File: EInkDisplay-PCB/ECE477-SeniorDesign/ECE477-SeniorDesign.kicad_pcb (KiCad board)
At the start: 4 copper layers, 89.2 x 77.8 mm, 95 parts, among them J1 Conn_01x05_Pin, J10 JST Conn, J12 JST Conn, J2 Conn_01x05_Pin, J3 Conn_01x05_Pin, J4 Conn_01x05_Pin, J6 Battery Connector, J7 USB_A, J8 JST Conn, J9 JST Conn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

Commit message: push
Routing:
- net /USB-UART/USB_D+: track 12.9 -> 24.9 mm, vias 1 -> 2
- net /USB-UART/USB_D-: track 11.4 -> 22.6 mm, vias 1 -> 2
- net VBUS: track 24.8 -> 35.3 mm, vias 0 -> 2
- net GND: track 99.3 -> 100.6 mm, vias 46 -> 47

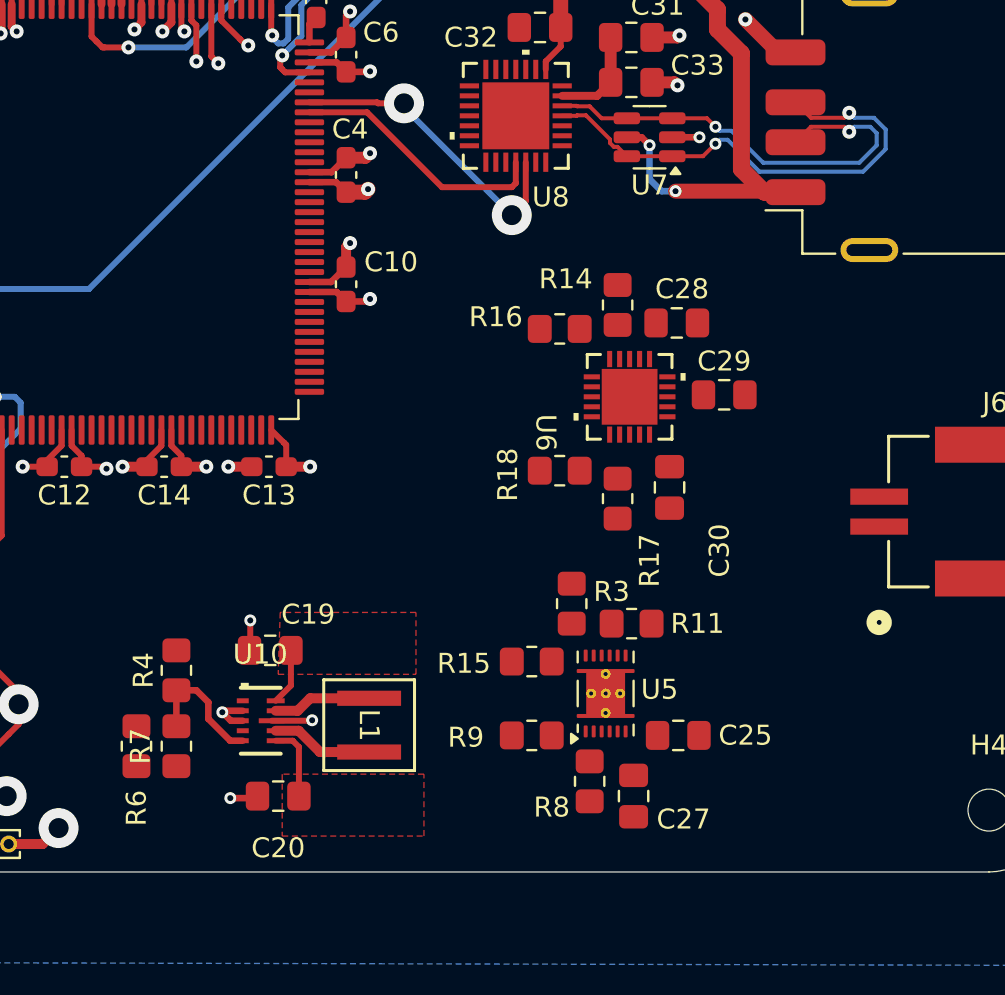
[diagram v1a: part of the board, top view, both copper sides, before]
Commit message: Power routing
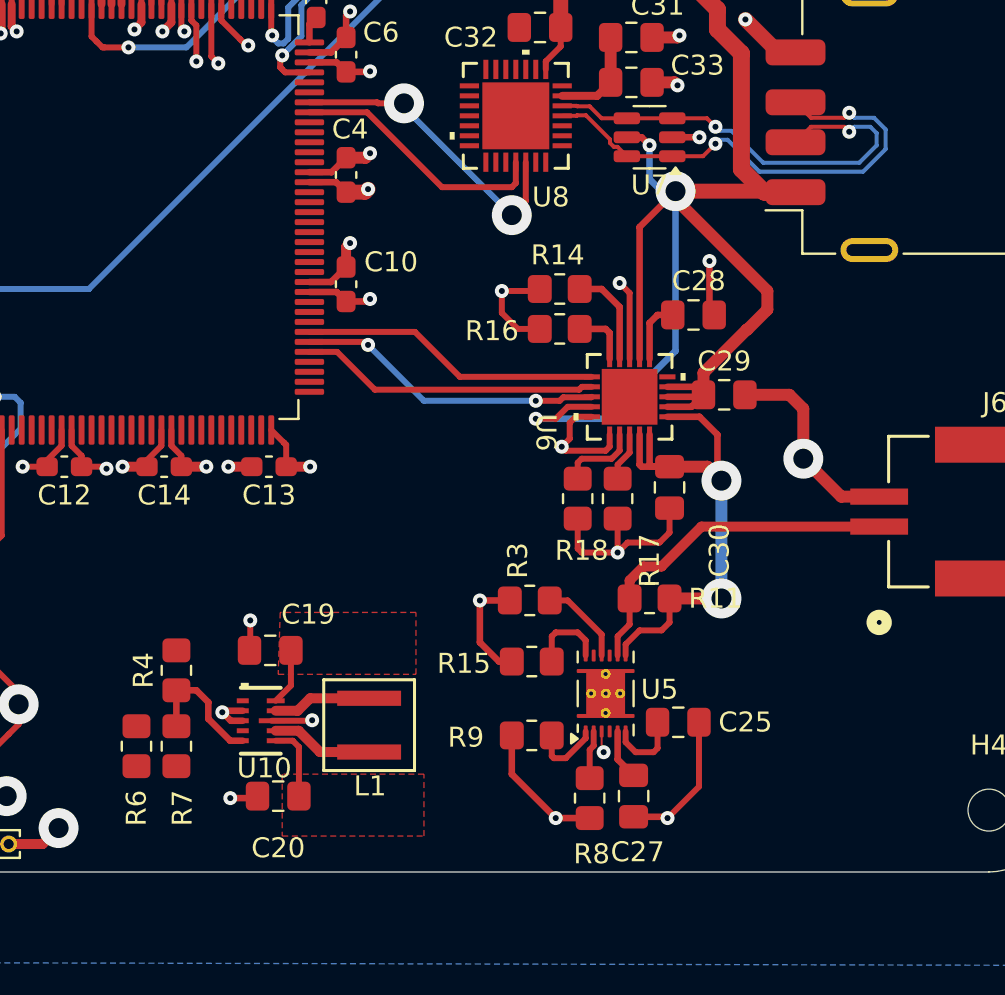
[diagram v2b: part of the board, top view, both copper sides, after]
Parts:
- moved R14 3.01 mm to (176.7, 93.6), turned to 0 degrees
- moved R3 2.11 mm to (175.2, 109.2), turned to 0 degrees
- moved R18 1.66 mm to (177.6, 104.1), turned to 90 degrees
- moved R11 1.55 mm to (181.2, 109.1)
- moved C28 0.93 mm to (183.4, 94.9)
- moved R8 0.84 mm to (178.2, 119.1)
- moved C25 0.66 mm to (182.6, 115.3)
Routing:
- net VBUS: track 35.3 -> 83.3 mm, vias 2 -> 3
- net GND: track 100.6 -> 146.6 mm, vias 47 -> 55
- net V_Batt: track 0.00 -> 27.3 mm, vias 0 -> 2
- net BATTERY_IN: track 0.00 -> 21.4 mm
- net /LipoPower/Recharge_ST1: track 0.00 -> 15.3 mm, vias 0 -> 2
- net /LipoPower/Recharge_PG: track 0.00 -> 15.1 mm
- net /LipoPower/Recharge_ST2: track 0.00 -> 15.0 mm
- net +3.3V: track 76.3 -> 88.6 mm, vias 23 -> 25
- net Net-(U6-PROG2): track 0.00 -> 4.98 mm
- net Net-(U5-BIN): track 0.00 -> 4.36 mm
- net /LipoPower/Monitor_GPOUT: track 0.00 -> 3.97 mm
- net Net-(U6-PROG3): track 0.00 -> 3.96 mm
- net /LipoPower/Monitor_SDA: track 0.00 -> 3.54 mm
- net V_5V: track 2.84 -> 6.04 mm
- net Net-(U6-THERM): track 0.00 -> 2.89 mm
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
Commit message: update
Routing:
- net V_5V: track 6.04 -> 45.8 mm, vias 0 -> 4
- net /LipoPower/Monitor_SCL: track 2.71 -> 36.8 mm, vias 0 -> 2
- net /LipoPower/Monitor_SDA: track 3.54 -> 36.2 mm, vias 0 -> 2
- net /LipoPower/Monitor_GPOUT: track 3.97 -> 34.1 mm, vias 0 -> 2
- net BATTERY_IN: track 21.4 -> 33.9 mm
- net Net-(U10-PG): track 0.00 -> 8.16 mm, vias 0 -> 2
- net +3.3V: track 88.6 -> 91.1 mm, vias 25 -> 26
- net GND: track 146.6 -> 149.0 mm
- net VBUS: track 83.3 -> 81.2 mm
- net Net-(U10-FB): track 6.66 -> 7.28 mm

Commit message: again
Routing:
- net V_5V: track 45.8 -> 52.3 mm
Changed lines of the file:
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@@
+	)
+	(segment
+		(start 163.2375 112.9)
+		(end 159.9 112.9)
+		(width 0.3)
+		(layer "F.Cu")
+		(net 17)
+	)
+	(segment
+		(start 162.475001 114.224998)
+		(end 163.075002 114.224998)
+		(width 0.3)
+		(layer "F.Cu")
+		(net 17)
 	)
 	(segment
@@
 		(end 182.3625 94.9625)
 		(width 0.33)
+		(layer "F.Cu")
+		(net 17)
+	)
+	(segment
+		(start 160.040244 114.22)
+		(end 160.045242 114.224998)
+		(width 0.3)
+		(layer "F.Cu")
+		(net 17)
+	)
+	(segment
+		(start 159.72 114.22)
+		(end 160.040244 114.22)
+		(width 0.3)
+		(layer "F.Cu")
+		(net 17)
+	)
+	(segment
+		(start 159.4 113.9)
+		(end 159.72 114.22)
+		(width 0.3)
 		(layer "F.Cu")
 		(net 17)
@@
 	)
 	(segment
+		(start 163.2375 112.9)
+		(end 163.2375 111.7)
+		(width 0.3)
+		(layer "F.Cu")
+		(net 17)
+	)
+	(segment
+		(start 159.9 112.9)
+		(end 159.4 113.4)
+		(width 0.3)
+		(layer "F.Cu")
+		(net 17)
+	)
+	(segment
 		(start 167.8 105.2)
 		(end 163.2375 109.7625)
@@
 	)
 	(segment
-		(start 162.475001 114.224998)
-		(end 163.2375 113.462499)
+		(start 159.4 113.4)
+		(end 159.4 113.9)
+		(width 0.3)
+		(layer "F.Cu")
+		(net 17)
+	)
+	(segment
+		(start 163.075002 114.224998)
+		(end 163.2375 114.0625)
 		(width 0.3)
 		(layer "F.Cu")
@@
 	)
 	(segment
-		(start 163.2375 113.462499)
-		(end 163.2375 111.7)
+		(start 181.6 94.9)
+		(end 182.3625 94.9)
+		(width 0.33)
+		(layer "F.Cu")
+		(net 17)
+	)
+	(segment
+		(start 160.045242 114.224998)
+		(end 160.824999 114.224998)
 		(width 0.3)
 		(layer "F.Cu")
@@
 	)
 	(segment
-		(start 181.6 94.9)
-		(end 182.3625 94.9)
-		(width 0.33)
+		(start 163.2375 114.0625)
+		(end 163.2375 112.9)
+		(width 0.3)
 		(layer "F.Cu")
 		(net 17)

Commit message: push
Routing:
- net GND: track 149.0 -> 161.8 mm, vias 55 -> 63
- net +3.3V: track 91.1 -> 94.2 mm, vias 26 -> 30
- net VBUS: track 81.2 -> 82.6 mm
- net V_5V: track 52.3 -> 51.0 mm, vias 4 -> 2
- net V_Batt: track 27.3 -> 26.4 mm
- net Net-(U10-FB): track 7.28 -> 7.83 mm

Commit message: push
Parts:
- moved R6 6.73 mm to (157.2, 110.0), turned to 0 degrees
- moved R7 2.53 mm to (157.9, 119.0)
- moved R4 2.48 mm to (157.9, 115.2)
- moved C20 1.03 mm to (162.2, 118.0)
- moved C19 0.70 mm to (161.9, 112.3)
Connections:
- R6 pad 1: +3.3V -> Net-(U10-PG)
- R6 pad 2: Net-(U10-PG) -> V_5V
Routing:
- net /USB-UART/USB_D-: track 22.6 -> 12.4 mm, vias 2 -> 0
- net /USB-UART/USB_D+: track 24.9 -> 15.8 mm
- net VBUS: track 82.6 -> 89.6 mm
- net I2C4_SDA: track 51.2 -> 56.9 mm
- net I2C4_SCL: track 52.2 -> 57.3 mm
- net +3.3V: track 94.2 -> 89.3 mm, vias 30 -> 32
- net Net-(U10-FB): track 7.83 -> 5.24 mm
- net BATTERY_IN: track 33.9 -> 31.9 mm
- net SPI2_MISO: track 46.5 -> 44.9 mm
- net SWCLK: track 45.7 -> 44.6 mm
- net V_5V: track 51.0 -> 50.0 mm
- net Net-(U10-PG): track 8.16 -> 9.05 mm
- net /LipoPower/Monitor_GPOUT: track 34.1 -> 34.9 mm
- net GND: track 161.8 -> 161.2 mm, vias 63 -> 71
- net /LipoPower/Monitor_SDA: track 36.2 -> 35.6 mm
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- added copper zone on F.Cu, net GND
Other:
- board text added: "ECE Team 7 Mark Hannah Cole Zoey"

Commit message: Sch update
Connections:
- U5 pad : (no net) -> GND
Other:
- board text removed: "ECE Team 7 Mark Hannah Cole Zoey"

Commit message: push
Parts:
- moved U5 0.09 mm to (179.0, 114.0)
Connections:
- U5 pad : GND -> (no net)
- U5 pad 13: unconnected-(U5-PAD-Pad13)_9 -> GND
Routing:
- net V_5V: track 50.0 -> 48.6 mm
